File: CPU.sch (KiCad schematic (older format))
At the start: 13 parts, among them P8 SWD, U1 STM32F40X_LQFP64, X1 8MHz 10ppm

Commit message: - removed 1 MOSFET of each group (no space) - removed 2 DC buffer caps (no space) - power stage routed - shunts and amps routed - post driver routed - pre driver HV routed
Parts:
- P8: footprint Pin_Headers:Pin_Header_Straight_2x03 -> Pin_Headers:Pin_Header_Straight_2x03_Pitch2.54mm
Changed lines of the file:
@@
 LIBS:contrib
 LIBS:valves
+LIBS:alexlib
 LIBS:Revolter-cache
 EELAYER 25 0
@@
 $EndComp
 $Comp
-L GND-RESCUE-BLDC_4 #PWR039
+L GND-RESCUE-BLDC_4 #PWR035
 U 1 1 53F757BC
 P 7750 6400
-F 0 "#PWR039" H 7750 6400 30  0001 C CNN
+F 0 "#PWR035" H 7750 6400 30  0001 C CNN
 F 1 "GND" H 7750 6330 30  0001 C CNN
 F 2 "" H 7750 6400 60  0001 C CNN
@@
 $EndComp
 $Comp
-L GND-RESCUE-BLDC_4 #PWR040
+L GND-RESCUE-BLDC_4 #PWR036
 U 1 1 53F757C8
 P 7200 5150
-F 0 "#PWR040" H 7200 5150 30  0001 C CNN
+F 0 "#PWR036" H 7200 5150 30  0001 C CNN
 F 1 "GND" H 7200 5080 30  0001 C CNN
 F 2 "" H 7200 5150 60  0001 C CNN
@@
 $EndComp
 $Comp
-L GND-RESCUE-BLDC_4 #PWR041
+L GND-RESCUE-BLDC_4 #PWR037
 U 1 1 53F757E9
 P 8250 1600
-F 0 "#PWR041" H 8250 1600 30  0001 C CNN
+F 0 "#PWR037" H 8250 1600 30  0001 C CNN
 F 1 "GND" H 8250 1530 30  0001 C CNN
 F 2 "" H 8250 1600 60  0001 C CNN
@@
 $EndComp
 $Comp
-L GND-RESCUE-BLDC_4 #PWR042
+L GND-RESCUE-BLDC_4 #PWR038
 U 1 1 53F757EF
 P 7150 2550
-F 0 "#PWR042" H 7150 2550 30  0001 C CNN
+F 0 "#PWR038" H 7150 2550 30  0001 C CNN
 F 1 "GND" H 7150 2480 30  0001 C CNN
 F 2 "" H 7150 2550 60  0001 C CNN
@@
 NoConn ~ 4500 5450
 $Comp
-L GND-RESCUE-BLDC_4 #PWR043
+L GND-RESCUE-BLDC_4 #PWR039
 U 1 1 53F75856
 P 7950 3300
-F 0 "#PWR043" H 7950 3300 30  0001 C CNN
+F 0 "#PWR039" H 7950 3300 30  0001 C CNN
 F 1 "GND" H 7950 3230 30  0001 C CNN
 F 2 "" H 7950 3300 60  0001 C CNN
@@
 F 0 "P8" V 10050 3150 60  0000 C CNN
 F 1 "SWD" V 10150 3150 60  0000 C CNN
-F 2 "Pin_Headers:Pin_Header_Straight_2x03" H 10100 3150 60  0001 C CNN
+F 2 "Pin_Headers:Pin_Header_Straight_2x03_Pitch2.54mm" H 10100 3150 60  0001 C CNN
 F 3 "" H 10100 3150 60  0001 C CNN
 	1    10100 3150
@@
 $EndComp
 $Comp
-L GND-RESCUE-BLDC_4 #PWR044
+L GND-RESCUE-BLDC_4 #PWR040
 U 1 1 53F7741D
 P 9600 3100
-F 0 "#PWR044" H 9600 3100 30  0001 C CNN
+F 0 "#PWR040" H 9600 3100 30  0001 C CNN
 F 1 "GND" H 9600 3030 30  0001 C CNN
 F 2 "" H 9600 3100 60  0001 C CNN
@@
 $EndComp
 $Comp
-L GND-RESCUE-BLDC_4 #PWR045
+L GND-RESCUE-BLDC_4 #PWR041
 U 1 1 53F7743B
 P 9100 1650
-F 0 "#PWR045" H 9100 1650 30  0001 C CNN
+F 0 "#PWR041" H 9100 1650 30  0001 C CNN
 F 1 "GND" H 9100 1580 30  0001 C CNN
 F 2 "" H 9100 1650 60  0001 C CNN
@@
 00 00 00 50 18 A4 4F 00 00 00 40 61 90 3E 01 00 00 00 85 41 FA 04 00 00 00 14 06 E9 13 00 00 00
 50 18 A4 4F 00 00 00 40 61 90 3E 01 00 00 00 85 41 FA 04 00 00 00 14 F6 FF 00 CF 05 3E 3D 48 21
-47 45 00 00 00 00 49 45 4E 44 AE 42 60 82 FA
+47 45 00 00 00 00 49 45 4E 44 AE 42 60 82 5B
 EndData
 $EndBitmap
@@
 9D 20 C6 37 81 40 20 10 08 04 02 81 D0 4E 10 E3 9B 40 20 10 08 04 02 81 40 68 27 88 F1 4D 20 10
 08 04 02 81 40 20 B4 13 C4 F8 26 10 08 04 02 81 40 20 10 DA 89 FF 07 6E 76 4C 5E B7 9B F3 6C 00
-00 00 00 49 45 4E 44 AE 42 60 82 E9
+00 00 00 49 45 4E 44 AE 42 60 82 24
 EndData
 $EndBitmap
@@
 $EndComp
 $Comp
-L GND-RESCUE-BLDC_4 #PWR046
+L GND-RESCUE-BLDC_4 #PWR042
 U 1 1 54097D19
 P 7750 2150
-F 0 "#PWR046" H 7750 2150 30  0001 C CNN
+F 0 "#PWR042" H 7750 2150 30  0001 C CNN
 F 1 "GND" H 7750 2080 30  0001 C CNN
 F 2 "" H 7750 2150 60  0001 C CNN
@@
 TX_SDA_NSS
 $Comp
-L +3V3 #PWR047
+L +3V3 #PWR043
 U 1 1 57529FFB
 P 7200 4200
-F 0 "#PWR047" H 7200 4050 50  0001 C CNN
+F 0 "#PWR043" H 7200 4050 50  0001 C CNN
 F 1 "+3V3" H 7200 4340 50  0000 C CNN
 F 2 "" H 7200 4200 50  0000 C CNN
@@
 $EndComp
 $Comp
-L +3V3 #PWR048
+L +3V3 #PWR044
 U 1 1 5752A2EE
 P 7400 5100
-F 0 "#PWR048" H 7400 4950 50  0001 C CNN
+F 0 "#PWR044" H 7400 4950 50  0001 C CNN
 F 1 "+3V3" H 7400 5240 50  0000 C CNN
 F 2 "" H 7400 5100 50  0000 C CNN
@@
 $EndComp
 $Comp
-L +3V3 #PWR049
+L +3V3 #PWR045
 U 1 1 5752A326
 P 7200 5350
-F 0 "#PWR049" H 7200 5200 50  0001 C CNN
+F 0 "#PWR045" H 7200 5200 50  0001 C CNN
 F 1 "+3V3" H 7050 5400 50  0000 C CNN
 F 2 "" H 7200 5350 50  0000 C CNN
@@
 $EndComp
 $Comp
-L +3V3 #PWR050
+L +3V3 #PWR046
 U 1 1 5752A907
 P 9750 2900
-F 0 "#PWR050" H 9750 2750 50  0001 C CNN
+F 0 "#PWR046" H 9750 2750 50  0001 C CNN
 F 1 "+3V3" V 9750 3150 50  0000 C CNN
 F 2 "" H 9750 2900 50  0000 C CNN
@@
 $EndComp
 $Comp
-L +3V3 #PWR051
+L +3V3 #PWR047
 U 1 1 5752A9C6
 P 9100 950
-F 0 "#PWR051" H 9100 800 50  0001 C CNN
+F 0 "#PWR047" H 9100 800 50  0001 C CNN
 F 1 "+3V3" H 9100 1090 50  0000 C CNN
 F 2 "" H 9100 950 50  0000 C CNN

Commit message: - updated project to 5.0.0 - added some more ignores
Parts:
- removed X1: 8MHz 10ppm, Crystals:Crystal_HC49-U_Vertical, symbol CRYSTAL_SMD
- added Y1: Crystal, Crystals:Crystal_HC49-U_Vertical, symbol Device:Crystal
- C17, C18, C19, C20, C21, C22, C23, C24, C25, C26: symbol C-RESCUE-BLDC_4 -> Revolter-rescue:C-RESCUE-BLDC_4
- P8: symbol CONN_6 -> Revolter-rescue:CONN_6
- U1: symbol STM32F40X_LQFP64 -> Revolter-rescue:STM32F40X_LQFP64
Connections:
- wire segments 53 -> 69
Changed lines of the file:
@@
-EESchema Schematic File Version 2
-LIBS:Revolter-rescue
-LIBS:power
-LIBS:device
-LIBS:transistors
-LIBS:conn
-LIBS:linear
-LIBS:regul
-LIBS:74xx
-LIBS:cmos4000
-LIBS:adc-dac
-LIBS:memory
-LIBS:xilinx
-LIBS:microcontrollers
-LIBS:dsp
-LIBS:microchip
-LIBS:analog_switches
-LIBS:motorola
-LIBS:texas
-LIBS:intel
-LIBS:audio
-LIBS:interface
-LIBS:digital-audio
-LIBS:philips
-LIBS:display
-LIBS:cypress
-LIBS:siliconi
-LIBS:opto
-LIBS:atmel
-LIBS:contrib
-LIBS:valves
-LIBS:alexlib
+EESchema Schematic File Version 4
 LIBS:Revolter-cache
-EELAYER 25 0
+EELAYER 26 0
 EELAYER END
 $Descr A4 11693 8268
@@
 $EndDescr
 $Comp
-L STM32F40X_LQFP64 U1
+L Revolter-rescue:STM32F40X_LQFP64 U1
 U 1 1 53F757A7
 P 5750 3900
@@
 $EndComp
 $Comp
-L C-RESCUE-BLDC_4 C19
+L Revolter-rescue:C-RESCUE-BLDC_4 C19
 U 1 1 53F757AE
 P 7500 6350
@@
 $EndComp
 $Comp
-L C-RESCUE-BLDC_4 C18
+L Revolter-rescue:C-RESCUE-BLDC_4 C18
 U 1 1 53F757B5
 P 7500 6100
@@
 $EndComp
 $Comp
-L GND-RESCUE-BLDC_4 #PWR039
+L Revolter-rescue:GND-RESCUE-BLDC_4 #PWR039
 U 1 1 53F757BC
 P 7750 6400
@@
 $EndComp
 $Comp
-L GND-RESCUE-BLDC_4 #PWR040
+L Revolter-rescue:GND-RESCUE-BLDC_4 #PWR040
 U 1 1 53F757C8
 P 7200 5150
@@
 $EndComp
 $Comp
-L C-RESCUE-BLDC_4 C17
+L Revolter-rescue:C-RESCUE-BLDC_4 C17
 U 1 1 53F757DB
 P 7350 1800
@@
 $EndComp
 $Comp
-L C-RESCUE-BLDC_4 C22
+L Revolter-rescue:C-RESCUE-BLDC_4 C22
 U 1 1 53F757E2
 P 8100 1800
@@
 $EndComp
 $Comp
-L GND-RESCUE-BLDC_4 #PWR041
+L Revolter-rescue:GND-RESCUE-BLDC_4 #PWR041
 U 1 1 53F757E9
 P 8250 1600
@@
 $EndComp
 $Comp
-L GND-RESCUE-BLDC_4 #PWR042
+L Revolter-rescue:GND-RESCUE-BLDC_4 #PWR042
 U 1 1 53F757EF
 P 7150 2550
@@
 SWCLK
 $Comp
-L C-RESCUE-BLDC_4 C20
+L Revolter-rescue:C-RESCUE-BLDC_4 C20
 U 1 1 53F757F8
 P 7750 5450
@@
 NoConn ~ 4500 5450
 $Comp
-L GND-RESCUE-BLDC_4 #PWR043
+L Revolter-rescue:GND-RESCUE-BLDC_4 #PWR043
 U 1 1 53F75856
 P 7950 3300
@@
 $EndComp
 Wire Wire Line
-	7950 3300 7950 3300
-Wire Wire Line
 	7200 5450 7200 5350
 Wire Wire Line
@@
 	7400 5650 7000 5650
 Wire Wire Line
-	7200 4200 7200 4650
+	7200 4200 7200 4350
 Wire Wire Line
 	7150 2350 7150 2550
@@
 	8100 1550 8100 1600
 Wire Wire Line
-	7350 1550 8250 1550
+	7350 1550 8100 1550
 Wire Wire Line
 	7350 1600 7350 1550
@@
 Connection ~ 8100 2050
 Wire Wire Line
-	7950 2050 8100 2050
+	7900 2050 8100 2050
 Wire Wire Line
-	8100 2000 8100 2250
+	8100 2000 8100 2050
 Wire Wire Line
 	7450 2250 7450 2150
@@
 	7450 2150 7000 2150
 Wire Wire Line
-	7000 2050 7550 2050
+	7000 2050 7350 2050
 Connection ~ 7200 4350
 Wire Wire Line
@@
 	7000 4950 7200 4950
 Wire Wire Line
-	7200 4950 7200 5150
+	7200 4950 7200 5050
 Wire Wire Line
-	7400 5100 7400 5650
+	7400 5100 7400 5150
 Connection ~ 7750 5750
 Wire Wire Line
@@
 Connection ~ 7750 6100
 Wire Wire Line
-	7750 5650 7750 6400
+	7750 5650 7750 5750
 Wire Wire Line
 	7750 6100 7700 6100
@@
 	7750 6350 7700 6350
 $Comp
-L C-RESCUE-BLDC_4 C21
+L Revolter-rescue:C-RESCUE-BLDC_4 C21
 U 1 1 53F75896
 P 7950 3100
@@
 NoConn ~ 4500 4850
 $Comp
-L CONN_6 P8
+L Revolter-rescue:CONN_6 P8
 U 1 1 53F77410
 P 10100 3150
@@
 $EndComp
 $Comp
-L GND-RESCUE-BLDC_4 #PWR044
+L Revolter-rescue:GND-RESCUE-BLDC_4 #PWR044
 U 1 1 53F7741D
 P 9600 3100
@@
 NRST
 $Comp
-L C-RESCUE-BLDC_4 C23
+L Revolter-rescue:C-RESCUE-BLDC_4 C23
 U 1 1 53F77426
 P 9400 1300
@@
 $EndComp
 $Comp
-L C-RESCUE-BLDC_4 C24
+L Revolter-rescue:C-RESCUE-BLDC_4 C24
 U 1 1 53F7742D
 P 9650 1300
@@
 $EndComp
 $Comp
-L GND-RESCUE-BLDC_4 #PWR045
+L Revolter-rescue:GND-RESCUE-BLDC_4 #PWR045
 U 1 1 53F7743B
 P 9100 1650
@@
 $EndComp
 $Comp
-L C-RESCUE-BLDC_4 C25
+L Revolter-rescue:C-RESCUE-BLDC_4 C25
 U 1 1 53F77447
 P 9900 1300
@@
 $EndComp
 $Comp
-L C-RESCUE-BLDC_4 C26
+L Revolter-rescue:C-RESCUE-BLDC_4 C26
 U 1 1 53F7744E
 P 10150 1300
@@
 $Bitmap
 Pos 1750 6700
-Scale 1,000000
+Scale 1.000000
 Data
 89 50 4E 47 0D 0A 1A 0A 00 00 00 0D 49 48 44 52 00 00 02 6A 00 00 02 41 08 02 00 00 00 79 DB 0E
@@
 $Bitmap
 Pos 3100 1050
-Scale 1,000000
+Scale 1.000000
 Data
 89 50 4E 47 0D 0A 1A 0A 00 00 00 0D 49 48 44 52 00 00 03 D4 00 00 00 CC 08 02 00 00 00 1D DB 7C
@@
 Text HLabel 4500 4950 0    60   Output ~ 0
 LED_GREEN
-$Comp
-L CRYSTAL_SMD X1
-U 1 1 540978A3
-P 7750 2050
-F 0 "X1" H 7750 2140 30  0000 C CNN
-F 1 "8MHz 10ppm" H 7800 1950 30  0000 L CNN
-F 2 "Crystals:Crystal_HC49-U_Vertical" H 7750 2050 60  0001 C CNN
-F 3 "" H 7750 2050 60  0000 C CNN
-F 4 "ABM3B-8.0-10-1UT" H 7750 2050 60  0001 C CNN "mfg#"
-	1    7750 2050
-	1    0    0    -1
-$EndComp
-$Comp
-L GND-RESCUE-BLDC_4 #PWR046
-U 1 1 54097D19
-P 7750 2150
-F 0 "#PWR046" H 7750 2150 30  0001 C CNN
-F 1 "GND" H 7750 2080 30  0001 C CNN
-F 2 "" H 7750 2150 60  0001 C CNN
-F 3 "" H 7750 2150 60  0001 C CNN
-	1    7750 2150
-	1    0    0    -1
-$EndComp
 Text HLabel 4500 2350 0    60   Input ~ 0
 MISO_ADC_EXT2
@@
 TX_SDA_NSS
 $Comp
-L +3V3 #PWR047
+L power:+3V3 #PWR047
 U 1 1 57529FFB
 P 7200 4200
@@
 $EndComp
 $Comp
-L +3V3 #PWR048
+L power:+3V3 #PWR048
 U 1 1 5752A2EE
 P 7400 5100
@@
 $EndComp
 $Comp
-L +3V3 #PWR049
+L power:+3V3 #PWR049
 U 1 1 5752A326
 P 7200 5350
@@
 $EndComp
 $Comp
-L +3V3 #PWR050
+L power:+3V3 #PWR050
 U 1 1 5752A907
 P 9750 2900
@@
 $EndComp
 $Comp
-L +3V3 #PWR051
+L power:+3V3 #PWR051
 U 1 1 5752A9C6
 P 9100 950
@@
 Connection ~ 7750 6350
 Wire Wire Line
-	9100 1000 10150 1000
+	9100 1000 9400 1000
+Wire Wire Line
+	9100 1600 9400 1600
+Wire Wire Line
+	7400 5150 7400 5650
+Wire Wire Line
+	8100 1550 8250 1550
+Wire Wire Line
+	7350 2050 7600 2050
+Wire Wire Line
+	8100 2050 8100 2250
+Wire Wire Line
+	7200 4350 7200 4450
+Wire Wire Line
+	7200 4450 7200 4550
 Wire Wire Line
-	9100 1600 10150 1600
+	7200 4550 7200 4650
+Wire Wire Line
+	7200 5050 7200 5150
+Wire Wire Line
+	7750 5750 7750 6100
+Wire Wire Line
+	7750 6100 7750 6350
+Wire Wire Line
+	9900 1600 10150 1600
+Wire Wire Line
+	9650 1600 9900 1600
+Wire Wire Line
+	9400 1600 9650 1600
+Wire Wire Line
+	9400 1000 9650 1000
+Wire Wire Line
+	9650 1000 9900 1000
+Wire Wire Line
+	9900 1000 10150 1000
+Wire Wire Line
+	7750 6350 7750 6400
+$Comp
+L Device:Crystal Y1
+U 1 1 5B683EEC
+P 7750 2050
+F 0 "Y1" H 7750 2318 50  0000 C CNN
+F 1 "Crystal" H 7750 2227 50  0000 C CNN
+F 2 "Crystals:Crystal_HC49-U_Vertical" H 7750 2050 50  0001 C CNN
+F 3 "~" H 7750 2050 50  0001 C CNN
+	1    7750 2050
+	1    0    0    -1
+$EndComp
 $EndSCHEMATC

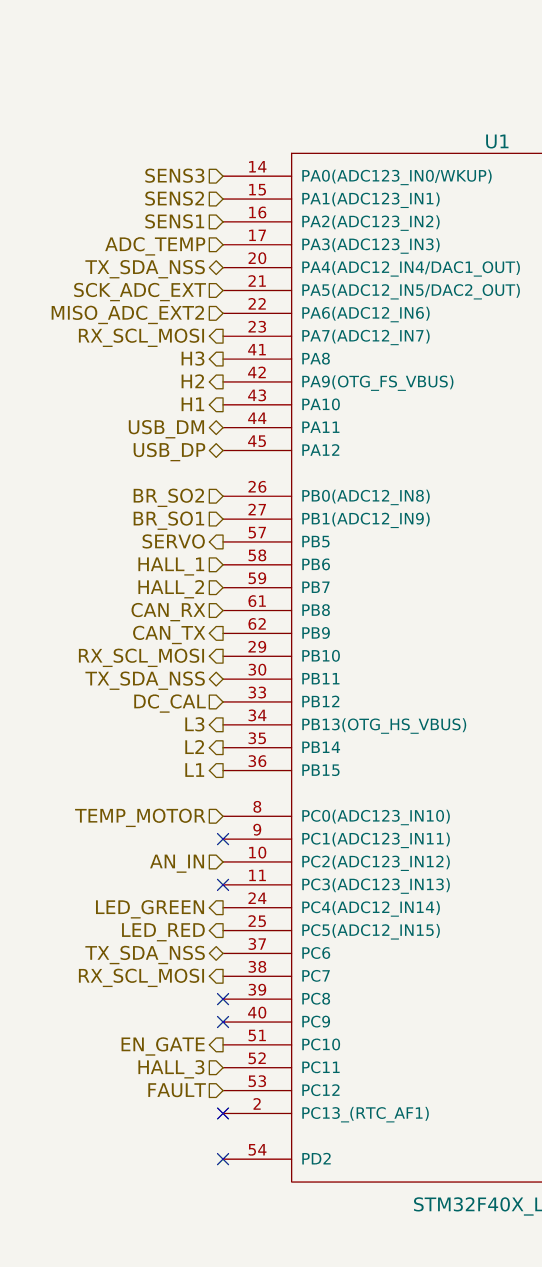
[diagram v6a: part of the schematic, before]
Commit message: - swapped TO220 dual MOSFET for single DualCool88 MOSFET package - removed postdriver - changed IRS2110 for IRS2186 - added third shunt - rewired CPU for VESC6 compatibility - layout completely from scratch
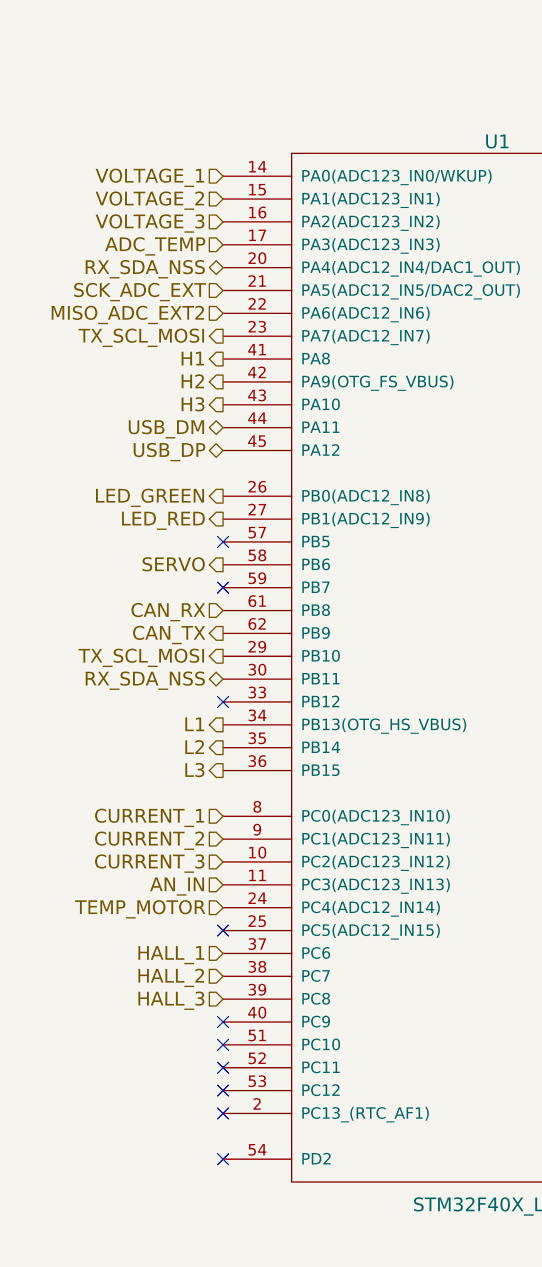
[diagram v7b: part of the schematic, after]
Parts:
- C17, C18, C19, C20, C21, C22, C23, C24, C25, C26: footprint Capacitors_SMD:C_0805 -> Capacitor_SMD:C_0805_2012Metric
- P8: footprint Pin_Headers:Pin_Header_Straight_2x03_Pitch2.54mm -> Connector_PinHeader_2.54mm:PinHeader_2x03_P2.54mm_Vertical
- U1: footprint Housings_QFP:LQFP-64_10x10mm_Pitch0.5mm -> Package_QFP:LQFP-64_10x10mm_P0.5mm
- Y1: footprint Crystals:Crystal_HC49-U_Vertical -> Crystal:Crystal_HC49-U_Vertical
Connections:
- net labels added: CURRENT_1, CURRENT_2, CURRENT_3, RX_SDA_NSS, TX_SCL_MOSI, VOLTAGE_1, VOLTAGE_2, VOLTAGE_3
- net labels removed: BR_SO1, BR_SO2, DC_CAL, EN_GATE, FAULT, RX_SCL_MOSI, SENS1, SENS2, SENS3, TX_SDA_NSS
- no-connect marks 13 -> 17
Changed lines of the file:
@@
 $Descr A4 11693 8268
 encoding utf-8
-Sheet 5 7
+Sheet 4 7
 Title "HSWR CPU"
 Date "2017-02-05"
@@
 F 0 "U1" H 5700 6200 60  0000 C CNN
 F 1 "STM32F40X_LQFP64" H 5750 1550 60  0000 C CNN
-F 2 "Housings_QFP:LQFP-64_10x10mm_Pitch0.5mm" H 5750 3900 60  0001 C CNN
+F 2 "Package_QFP:LQFP-64_10x10mm_P0.5mm" H 5750 3900 60  0001 C CNN
 F 3 "" H 5750 3900 60  0001 C CNN
 	1    5750 3900
@@
 F 0 "C19" H 7550 6450 50  0000 L CNN
 F 1 "1u" H 7550 6250 50  0000 L CNN
-F 2 "Capacitors_SMD:C_0805" H 7500 6350 60  0001 C CNN
+F 2 "Capacitor_SMD:C_0805_2012Metric" H 7500 6350 60  0001 C CNN
 F 3 "" H 7500 6350 60  0001 C CNN
 	1    7500 6350
@@
 F 0 "C18" H 7550 6200 50  0000 L CNN
 F 1 "1u" H 7550 6000 50  0000 L CNN
-F 2 "Capacitors_SMD:C_0805" H 7500 6100 60  0001 C CNN
+F 2 "Capacitor_SMD:C_0805_2012Metric" H 7500 6100 60  0001 C CNN
 F 3 "" H 7500 6100 60  0001 C CNN
 	1    7500 6100
@@
 F 0 "C17" H 7400 1900 50  0000 L CNN
 F 1 "15p" H 7400 1700 50  0000 L CNN
-F 2 "Capacitors_SMD:C_0805" H 7350 1800 60  0001 C CNN
+F 2 "Capacitor_SMD:C_0805_2012Metric" H 7350 1800 60  0001 C CNN
 F 3 "" H 7350 1800 60  0001 C CNN
 	1    7350 1800
@@
 F 0 "C22" H 8150 1900 50  0000 L CNN
 F 1 "15p" H 8150 1700 50  0000 L CNN
-F 2 "Capacitors_SMD:C_0805" H 8100 1800 60  0001 C CNN
+F 2 "Capacitor_SMD:C_0805_2012Metric" H 8100 1800 60  0001 C CNN
 F 3 "" H 8100 1800 60  0001 C CNN
 	1    8100 1800
@@
 F 0 "C20" H 7800 5550 50  0000 L CNN
 F 1 "1u" H 7800 5350 50  0000 L CNN
-F 2 "Capacitors_SMD:C_0805" H 7750 5450 60  0001 C CNN
+F 2 "Capacitor_SMD:C_0805_2012Metric" H 7750 5450 60  0001 C CNN
 F 3 "" H 7750 5450 60  0001 C CNN
 	1    7750 5450
@@
 NoConn ~ 4500 6050
 NoConn ~ 4500 5850
-NoConn ~ 4500 5350
+NoConn ~ 4500 5050
 NoConn ~ 4500 5450
 $Comp
@@
 F 0 "C21" H 8000 3200 50  0000 L CNN
 F 1 "10n" H 8000 3000 50  0000 L CNN
-F 2 "Capacitors_SMD:C_0805" H 7950 3100 60  0001 C CNN
+F 2 "Capacitor_SMD:C_0805_2012Metric" H 7950 3100 60  0001 C CNN
 F 3 "" H 7950 3100 60  0001 C CNN
 	1    7950 3100
@@
 $EndComp
 NoConn ~ 7000 3300
-NoConn ~ 4500 4650
-NoConn ~ 4500 4850
 $Comp
 L Revolter-rescue:CONN_6 P8
@@
 F 0 "P8" V 10050 3150 60  0000 C CNN
 F 1 "SWD" V 10150 3150 60  0000 C CNN
-F 2 "Pin_Headers:Pin_Header_Straight_2x03_Pitch2.54mm" H 10100 3150 60  0001 C CNN
+F 2 "Connector_PinHeader_2.54mm:PinHeader_2x03_P2.54mm_Vertical" H 10100 3150 60  0001 C CNN
 F 3 "" H 10100 3150 60  0001 C CNN
 	1    10100 3150
@@
 F 0 "C23" H 9450 1400 50  0000 L CNN
 F 1 "1u" H 9450 1200 50  0000 L CNN
-F 2 "Capacitors_SMD:C_0805" H 9400 1300 60  0001 C CNN
+F 2 "Capacitor_SMD:C_0805_2012Metric" H 9400 1300 60  0001 C CNN
 F 3 "" H 9400 1300 60  0001 C CNN
 	1    9400 1300
@@
 F 0 "C24" H 9700 1400 50  0000 L CNN
 F 1 "1u" H 9700 1200 50  0000 L CNN
-F 2 "Capacitors_SMD:C_0805" H 9650 1300 60  0001 C CNN
+F 2 "Capacitor_SMD:C_0805_2012Metric" H 9650 1300 60  0001 C CNN
 F 3 "" H 9650 1300 60  0001 C CNN
 	1    9650 1300
@@
 F 0 "C25" H 9950 1400 50  0000 L CNN
 F 1 "1u" H 9950 1200 50  0000 L CNN
-F 2 "Capacitors_SMD:C_0805" H 9900 1300 60  0001 C CNN
+F 2 "Capacitor_SMD:C_0805_2012Metric" H 9900 1300 60  0001 C CNN
 F 3 "" H 9900 1300 60  0001 C CNN
 	1    9900 1300
@@
 F 0 "C26" H 10200 1400 50  0000 L CNN
 F 1 "1u" H 10200 1200 50  0000 L CNN
-F 2 "Capacitors_SMD:C_0805" H 10150 1300 60  0001 C CNN
+F 2 "Capacitor_SMD:C_0805_2012Metric" H 10150 1300 60  0001 C CNN
 F 3 "" H 10150 1300 60  0001 C CNN
 	1    10150 1300
@@
 Text HLabel 4500 2950 0    60   BiDi ~ 0
 USB_DP
-Text HLabel 4500 3350 0    60   Output ~ 0
+Text HLabel 4500 3450 0    60   Output ~ 0
 SERVO
-Text HLabel 4500 3450 0    60   Input ~ 0
+Text HLabel 4500 5150 0    60   Input ~ 0
 HALL_1
-Text HLabel 4500 3550 0    60   Input ~ 0
+Text HLabel 4500 5250 0    60   Input ~ 0
 HALL_2
-Text HLabel 4500 5650 0    60   Input ~ 0
-HALL_3
 Text HLabel 4500 3850 0    60   Output ~ 0
-RX_SCL_MOSI
+TX_SCL_MOSI
 Text HLabel 4500 3950 0    60   3State ~ 0
-TX_SDA_NSS
-Text HLabel 4500 4550 0    60   Input ~ 0
+RX_SDA_NSS
+Text HLabel 4500 4950 0    60   Input ~ 0
 TEMP_MOTOR
-Text HLabel 4500 4150 0    60   Output ~ 0
+Text HLabel 4500 4350 0    60   Output ~ 0
 L3
 Text HLabel 4500 4250 0    60   Output ~ 0
 L2
-Text HLabel 4500 4350 0    60   Output ~ 0
+Text HLabel 4500 4150 0    60   Output ~ 0
 L1
 Text HLabel 4500 2250 0    60   Input ~ 0
 SCK_ADC_EXT
-Text HLabel 4500 5150 0    60   3State ~ 0
-TX_SDA_NSS
-Text HLabel 4500 5250 0    60   Output ~ 0
-RX_SCL_MOSI
-Text HLabel 4500 5750 0    60   Input ~ 0
-FAULT
 Text HLabel 4500 2550 0    60   Output ~ 0
-H3
+H1
 Text HLabel 4500 2650 0    60   Output ~ 0
 H2
 Text HLabel 4500 2750 0    60   Output ~ 0
-H1
-Text HLabel 4500 1750 0    60   Input ~ 0
-SENS3
-Text HLabel 4500 1850 0    60   Input ~ 0
-SENS2
+H3
 Text HLabel 4500 1950 0    60   Input ~ 0
-SENS1
-Text HLabel 4500 3250 0    60   Input ~ 0
-BR_SO1
-Text HLabel 4500 3150 0    60   Input ~ 0
-BR_SO2
-Text HLabel 4500 4750 0    60   Input ~ 0
+VOLTAGE_3
+Text HLabel 4500 1850 0    60   Input ~ 0
+VOLTAGE_2
+Text HLabel 4500 1750 0    60   Input ~ 0
+VOLTAGE_1
+Text HLabel 4500 4550 0    60   Input ~ 0
+CURRENT_1
+Text HLabel 4500 4850 0    60   Input ~ 0
 AN_IN
-Text HLabel 4500 5550 0    60   Output ~ 0
-EN_GATE
-Text HLabel 4500 4050 0    60   Input ~ 0
-DC_CAL
 Wire Notes Line
 	9250 2650 9250 3550
@@
 Text HLabel 4500 3750 0    60   Output ~ 0
 CAN_TX
-Text HLabel 4500 5050 0    60   Output ~ 0
+Text HLabel 4500 3250 0    60   Output ~ 0
 LED_RED
-Text HLabel 4500 4950 0    60   Output ~ 0
+Text HLabel 4500 3150 0    60   Output ~ 0
 LED_GREEN
 Text HLabel 4500 2350 0    60   Input ~ 0
 MISO_ADC_EXT2
 Text HLabel 4500 2450 0    60   Output ~ 0
-RX_SCL_MOSI
+TX_SCL_MOSI
 Text HLabel 4500 2050 0    60   Input ~ 0
 ADC_TEMP
 Text HLabel 4500 2150 0    60   3State ~ 0
-TX_SDA_NSS
+RX_SDA_NSS
 $Comp
 L power:+3V3 #PWR047
@@
 F 0 "Y1" H 7750 2318 50  0000 C CNN
 F 1 "Crystal" H 7750 2227 50  0000 C CNN
-F 2 "Crystals:Crystal_HC49-U_Vertical" H 7750 2050 50  0001 C CNN
+F 2 "Crystal:Crystal_HC49-U_Vertical" H 7750 2050 50  0001 C CNN
 F 3 "~" H 7750 2050 50  0001 C CNN
 	1    7750 2050
 	1    0    0    -1
 $EndComp
+NoConn ~ 4500 3350
+NoConn ~ 4500 3550
+NoConn ~ 4500 4050
+Text HLabel 4500 4650 0    60   Input ~ 0
+CURRENT_2
+Text HLabel 4500 4750 0    60   Input ~ 0
+CURRENT_3
+Text HLabel 4500 5350 0    60   Input ~ 0
+HALL_3
+NoConn ~ 4500 5550
+NoConn ~ 4500 5750
+NoConn ~ 4500 5650
 $EndSCHEMATC
